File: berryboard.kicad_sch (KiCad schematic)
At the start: 46 parts, among them J1 XT30_SERVO_PWR, J12 QWIIC_RPI_1, J13 QWIIC_RPI_2, J14 QWIIC_RPI_3, J15 QWIIC_MCU_1, J16 QWIIC_MCU_2, J17 QWIIC_MCU_3, J18 LEAK_1, J19 LEAK_2, J2 RPi_GPIO_40P, J20 HAT_5V_IN, J21 SWD, J3 USB_C_RP2350, J4 SERVO_SIG, J5 SERVO_PWR, J6 SERVO_GND, U1 TPS2121, U2 AP2112K-3.3, U3 ICM-42688-P, U4 MMC5983MA, U5 24LC32, U6 RP2350B, U7 W25Q16JVSS

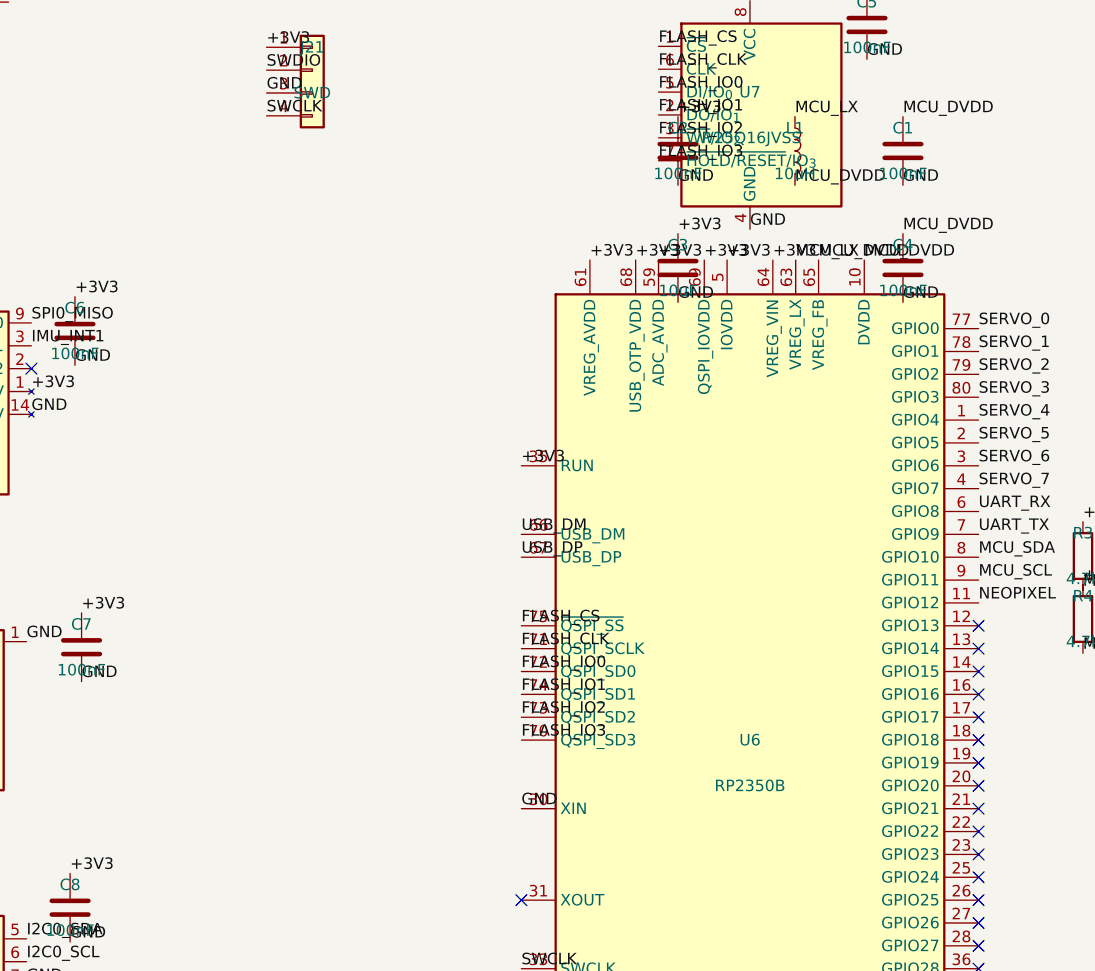
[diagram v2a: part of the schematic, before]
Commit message: RP2350B design rules compliance: SMPS, USB termination, crystal circuit
Changes to bring schematic into full compliance with Raspberry Pi Foundation
"Hardware design with RP2350" guide (build 2024-10-15):

SMPS (Chapter 2):
- L1: change inductor from generic 10uH/0603 to mandated Abracon
  AOTA-B201610S3R3-101-T 3.3uH in 0806 (2016 metric) package.
  This specific polarized part is required; any substitution risks
  switching regulator instability.
- C2 (VREG_VIN input cap): 100nF → 4.7uF per spec (0402 retained)
- C4 (MCU_DVDD / VREG_LX output cap): 100nF → 4.7uF per spec (0402 retained)
- VREG_AVDD filter: VREG_AVDD was directly tied to +3V3; now routed
  through R12 (33Ω) + C15 (4.7uF) RC filter to new net MCU_AVDD.
  VREG_AVDD is analog-sensitive and must not connect directly to +3V3.

USB termination (Chapter 5.1):
- Added R9 and R10 (27Ω 0402) in series on USB_DP and USB_DM
  respectively, placed between U6 and J3 (USB-C connector).
  Net renamed: USB_DP_MCU / USB_DM_MCU on chip side; USB_DP / USB_DM
  on connector side, maintaining compatibility with existing wiring.

Crystal oscillator (Chapter 4):
- Added Y1: Abracon ABM8-272-T3, 12MHz, footprint Crystal_SMD_3225-4Pin_3.2x2.5mm
- Added C13 (15pF, XIN load cap) and C14 (15pF, XOUT load cap)
- Added R11 (1kΩ) in series on XOUT between U6 and crystal.
  This prevents over-driving the crystal at 3.3V IOVDD.
- Crystal circuit required for USB full-speed timing compliance.

Crystal nets: XIN, XOUT (crystal side), XOUT_MCU (chip side of R11)

Co-Authored-By: Claude Sonnet 4.6 <noreply@anthropic.com>
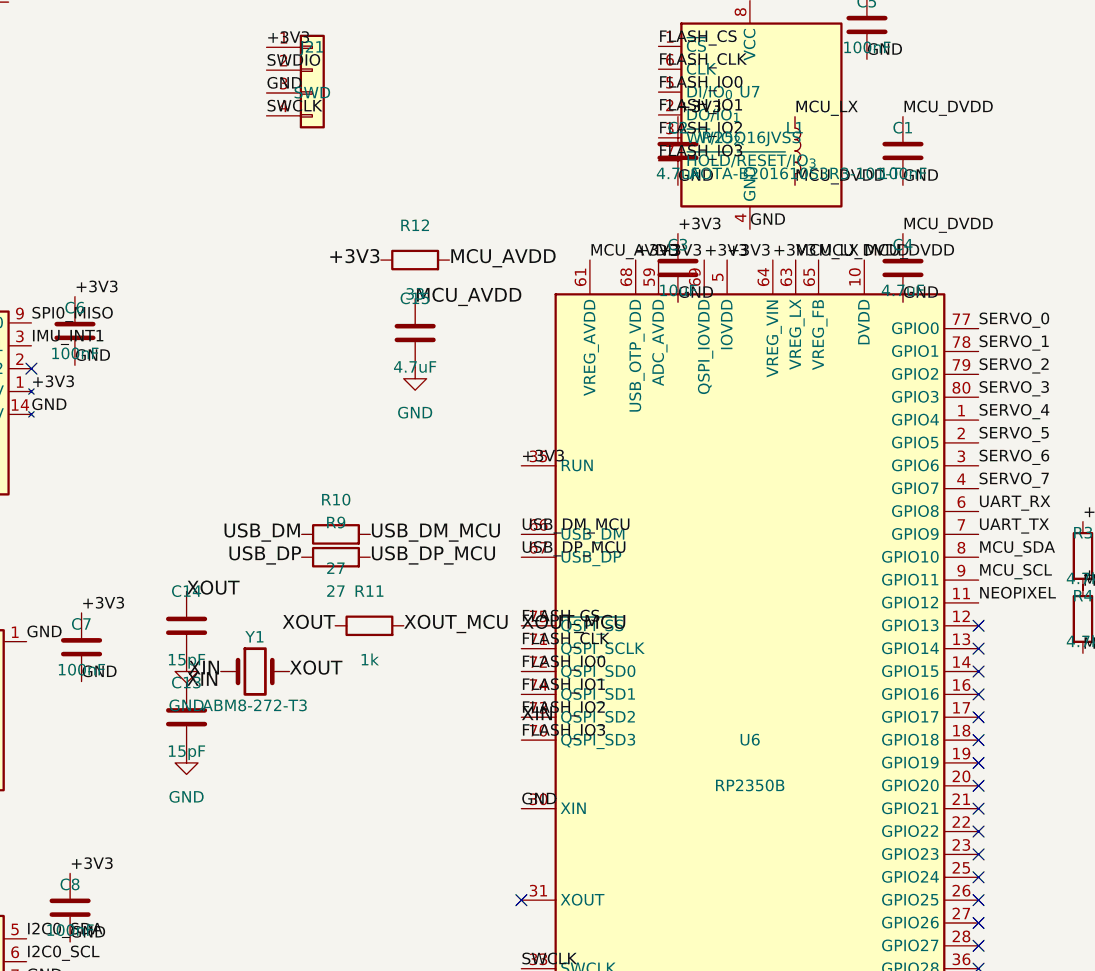
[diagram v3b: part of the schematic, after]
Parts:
- added C13, C14: 15pF, Capacitor_SMD:C_0402_1005Metric, symbol Device:C
- added C15: 4.7uF, Capacitor_SMD:C_0402_1005Metric, symbol Device:C
- added R10, R9: 27, Resistor_SMD:R_0402_1005Metric, symbol Device:R
- added R11: 1k, Resistor_SMD:R_0402_1005Metric, symbol Device:R
- added R12: 33, Resistor_SMD:R_0402_1005Metric, symbol Device:R
- added Y1: ABM8-272-T3, Crystal:Crystal_SMD_3225-4Pin_3.2x2.5mm, symbol Device:Crystal
- C2, C4: value 100nF -> 4.7uF
- L1: value 10uH -> AOTA-B201610S3R3-101-T; footprint Inductor_SMD:L_0603_1608Metric -> Inductor_SMD:L_0806_2016Metric
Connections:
- net +3V3: now also R12.1; no longer U6.61 (VREG_AVDD)
- net FLASH_CS: now also R11.2
- net FLASH_IO2: now also C13.1, Y1.1
- net GND: now also C13.2, C14.2, C15.2
- net USB_DM: now also R10.1; no longer U6.66 (USB_DM)
- net USB_DP: now also R9.1; no longer U6.67 (USB_DP)
- new net MCU_AVDD: C15.1, R12.2, U6.61 (VREG_AVDD)
- new net USB_DM_MCU: R10.2, U6.66 (USB_DM)
- new net USB_DP_MCU: R9.2, U6.67 (USB_DP)
- new net XOUT: C14.1, R11.1, Y1.2

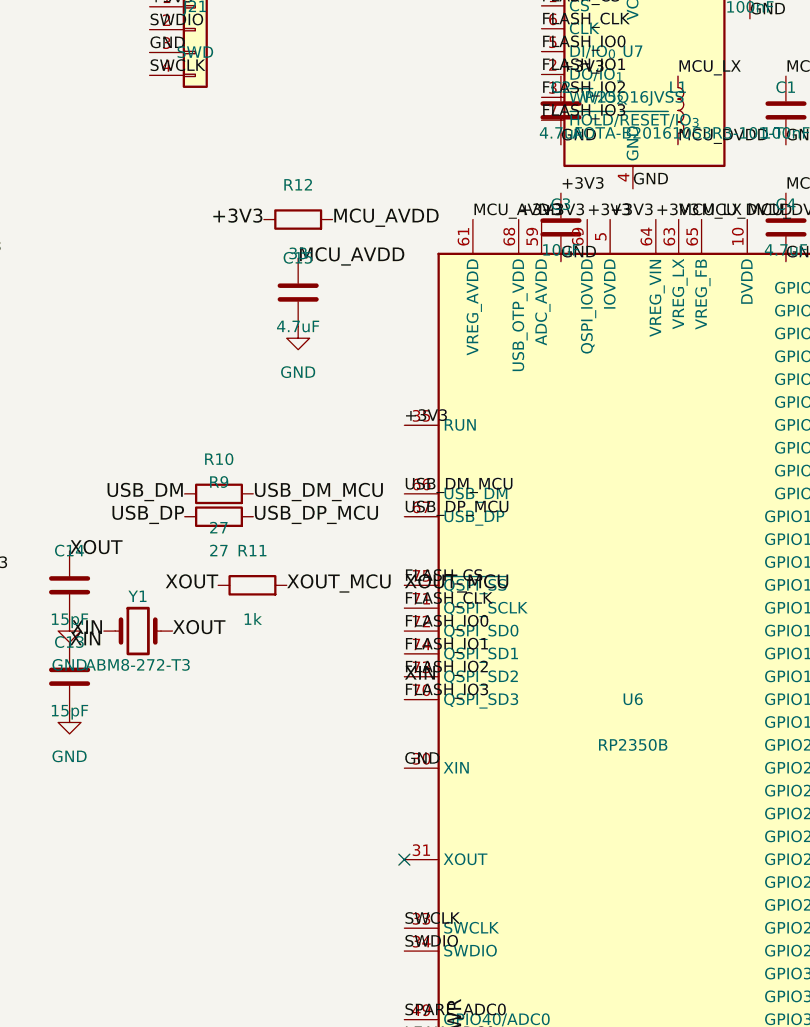
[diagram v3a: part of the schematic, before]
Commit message: Place all design-guide-critical components near U6
Per the RP2350 Hardware Design Guide:

USB resistors (27Ω series on USB_DP/DM):
- R9 → (153.5, 94.0) — 2.8mm from USB_DP pin 67
- R10 → (156.5, 94.0) — 2.8mm from USB_DM pin 66

SMPS switching regulator components:
- L1 (3.3µH Abracon inductor) → (156.24, 91.5) — between VREG_VIN/LX pads
- C2 (4.7µF VREG cap) → (154.5, 90.0) — near L1/VREG pins
- C4 (4.7µF VREG cap) → (158.0, 90.0) — near L1/VREG pins
- R12 (33Ω VREG_AVDD filter) → (159.5, 93.5) — close to VREG_AVDD pin 61
- C15 (4.7µF VREG_AVDD cap) → (159.5, 91.5) — after R12 on filtered rail

Crystal oscillator components:
- C13 (15pF XIN load cap) → (151.0, 108.5) — 3.1mm from XIN pin 30
- C14 (15pF XOUT load cap) → (155.0, 108.5) — 2.5mm from XOUT pin 31
- R11 (1kΩ XOUT series) → (155.5, 110.5) — between XOUT and crystal
- Y1 (12MHz crystal) → (153.44, 114.0) — centered below XIN/XOUT pins

Schematic changes (from prior session):
- Correct FLASH/QSPI labels on U6: FLASH_IO3..IO0, FLASH_CLK, FLASH_CS
  at proper pin positions using correct Y-inversion formula
- Add XIN/XOUT_MCU labels on U6 to connect crystal oscillator circuit
- Add PWR_FLAG on MCU_AVDD net to resolve VREG_AVDD ERC error
- Update L1 footprint to Inductor_SMD:L_Wuerth_PMCI-201610 (same
  2.0x1.6mm body as the Abracon AOTA-B201610S3R3-101-T)
- Sync new components (R9, R10, R11, R12, C13, C14, C15, Y1) to PCB

Co-Authored-By: Claude Sonnet 4.6 <noreply@anthropic.com>
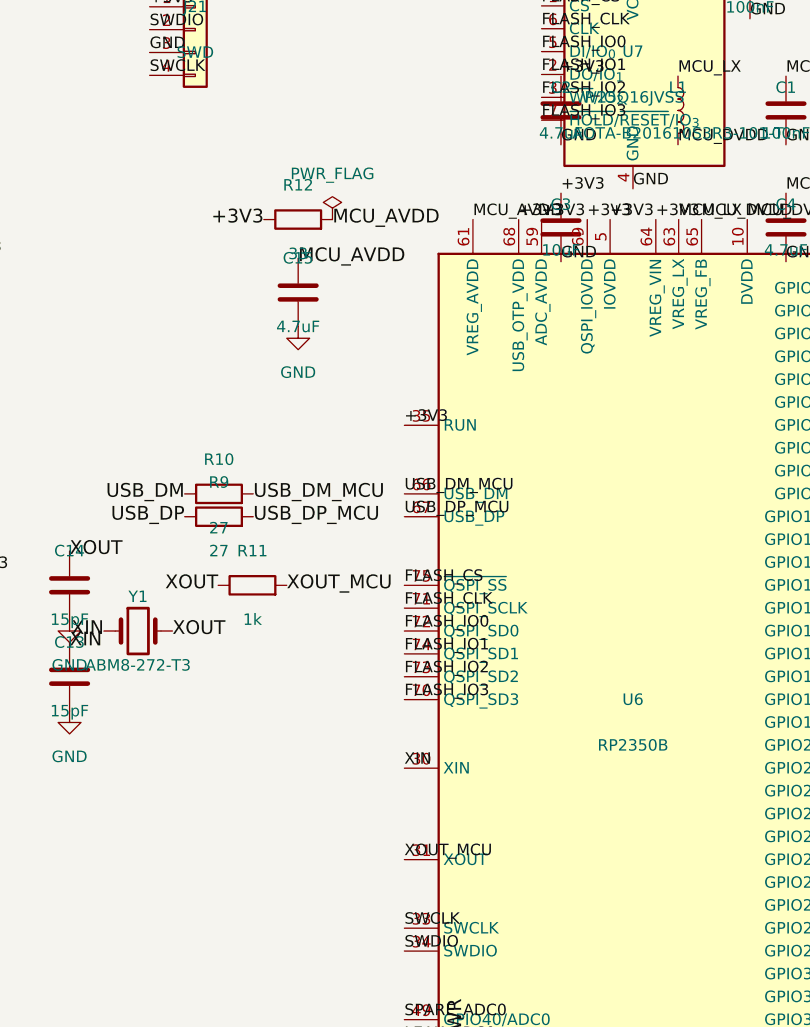
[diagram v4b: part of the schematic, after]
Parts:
- L1: footprint Inductor_SMD:L_0806_2016Metric -> Inductor_SMD:L_Wuerth_PMCI-201610
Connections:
- net FLASH_CS: no longer R11.2
- net FLASH_IO2: no longer C13.1, Y1.1
- net GND: no longer U6.30 (XIN)
- net XOUT_MCU: now reaches U6.31 (XOUT)
- net XOUT_MCU: now also R11.2
- new net XIN: C13.1, U6.30 (XIN), Y1.1
- no-connect marks 52 -> 51
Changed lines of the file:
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@@
 	)
 	(no_connect
-		(at 189.6 125.24)
-	)
-	(no_connect
 		(at 29.62 104.92)
 	)
@@
 		)
 	)
-	(label "FLASH_IO1"
-		(at 189.6 102.38 0)
-		(effects
-			(font
-				(size 1.27 1.27)
-			)
-			(justify left bottom)
-		)
-	)
 	(label "SERVO_PWR"
 		(at 269.24 49.53 0)
@@
 		)
 	)
-	(label "FLASH_CLK"
-		(at 189.6 97.3 0)
-		(effects
-			(font
-				(size 1.27 1.27)
-			)
-			(justify left bottom)
-		)
-	)
 	(label "+5V"
 		(at 87.63 166.37 0)
@@
 		)
 	)
-	(label "FLASH_IO2"
-		(at 189.6 104.92 0)
-		(effects
-			(font
-				(size 1.27 1.27)
-			)
-			(justify left bottom)
-		)
-	)
 	(label "I2C0_SDA"
 		(at 134.62 129.54 0)
@@
 	)
 	(label "GND"
-		(at 189.6 115.08 0)
-		(effects
-			(font
-				(size 1.27 1.27)
-			)
-			(justify left bottom)
-		)
-	)
-	(label "GND"
 		(at 118.11 191.77 0)
 		(effects
@@
 		)
 	)
-	(label "FLASH_IO3"
-		(at 189.6 107.46 0)
-		(effects
-			(font
-				(size 1.27 1.27)
-			)
-			(justify left bottom)
-		)
-	)
 	(label "UART_RX"
 		(at 29.62 97.3 0)
@@
 		)
 	)
-	(label "FLASH_CS"
-		(at 189.6 94.76 0)
-		(effects
-			(font
-				(size 1.27 1.27)
-			)
-			(justify left bottom)
-		)
-	)
 	(label "I2C0_SCL"
 		(at 29.62 120.16 0)
@@
 		)
 	)
-	(label "FLASH_IO0"
-		(at 189.6 99.84 0)
-		(effects
-			(font
-				(size 1.27 1.27)
-			)
-			(justify left bottom)
-		)
-	)
 	(label "GND"
 		(at 87.63 181.61 0)
@@
 			)
 		)
-		(property "Footprint" "Inductor_SMD:L_0806_2016Metric"
+		(property "Footprint" "Inductor_SMD:L_Wuerth_PMCI-201610"
 			(at 220 42 0)
 			(hide yes)
@@
 		(effects (font (size 1.524 1.524)))
 	)
-	(label "XIN"
-		(at 189.6 104.92 0)
-		(effects (font (size 1.524 1.524)))
-	)
-	(label "XOUT_MCU"
-		(at 189.6 94.76 0)
-		(effects (font (size 1.524 1.524)))
-	)
 	(label "XOUT_MCU"
 		(at 176.53 94.76 0)
@@
 				)
 			)
+		)
+	)
+	(label "FLASH_IO3"
+		(at 189.6 107.46 0)
+		(effects
+			(font
+				(size 1.27 1.27)
+			)
+			(justify left bottom)
+		)
+	)
+	(label "FLASH_IO2"
+		(at 189.6 104.92 0)
+		(effects
+			(font
+				(size 1.27 1.27)
+			)
+			(justify left bottom)
+		)
+	)
+	(label "FLASH_IO1"
+		(at 189.6 102.38 0)
+		(effects
+			(font
+				(size 1.27 1.27)
+			)
+			(justify left bottom)
+		)
+	)
+	(label "FLASH_IO0"
+		(at 189.6 99.84 0)
+		(effects
+			(font
+				(size 1.27 1.27)
+			)
+			(justify left bottom)
+		)
+	)
+	(label "FLASH_CLK"
+		(at 189.6 97.3 0)
+		(effects
+			(font
+				(size 1.27 1.27)
+			)
+			(justify left bottom)
+		)
+	)
+	(label "FLASH_CS"
+		(at 189.6 94.76 0)
+		(effects
+			(font
+				(size 1.27 1.27)
+			)
+			(justify left bottom)
+		)
+	)
+	(label "XIN"
+		(at 189.6 115.08 0)
+		(effects
+			(font
+				(size 1.27 1.27)
+			)
+			(justify left bottom)
+		)
+	)
+	(label "XOUT_MCU"
+		(at 189.6 125.24 0)
+		(effects
+			(font
+				(size 1.27 1.27)
+			)
+			(justify left bottom)
+		)
+	)
+	(symbol
+		(lib_id "power:PWR_FLAG")
+		(at 181.61 54.12 0)
+		(unit 1)
+		(exclude_from_sim no)
+		(in_bom yes)
+		(on_board yes)
+		(dnp no)
+		(property "Reference" "#PWR7b84"
+			(at 181.61 47.77 0)
+			(effects (font (size 1.27 1.27)) (hide yes))
+		)
+		(property "Value" "PWR_FLAG"
+			(at 181.61 49.04 0)
+			(effects (font (size 1.27 1.27)))
+		)
+		(property "Footprint" ""
+			(at 181.61 54.12 0)
+			(effects (font (size 1.27 1.27)) (hide yes))
+		)
+		(property "Datasheet" "~"
+			(at 181.61 54.12 0)
+			(effects (font (size 1.27 1.27)) (hide yes))
+		)
+		(instances
+			(project "berryboard"
+				(path "/ff3b3dad-4bf5-4947-8010-24cd58ee7f98"
+					(reference "#PWR7b84") (unit 1)
+				)
+			)
